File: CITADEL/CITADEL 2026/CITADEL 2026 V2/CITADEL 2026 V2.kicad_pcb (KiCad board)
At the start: 2 copper layers, 141.5 x 109.7 mm, 68 parts, among them J1 FAERIE CAN BUS, J10 ESC PWR, J13 SERVO DAUGHTER, J2 CITADEL CAN BUS, J3 FAERIE 12V, J4 CITADEL BATTERY, J5 FAERIE BATTERY, J6 LED STRIP, J7 CAMERA 1, J8 CAMERA 2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

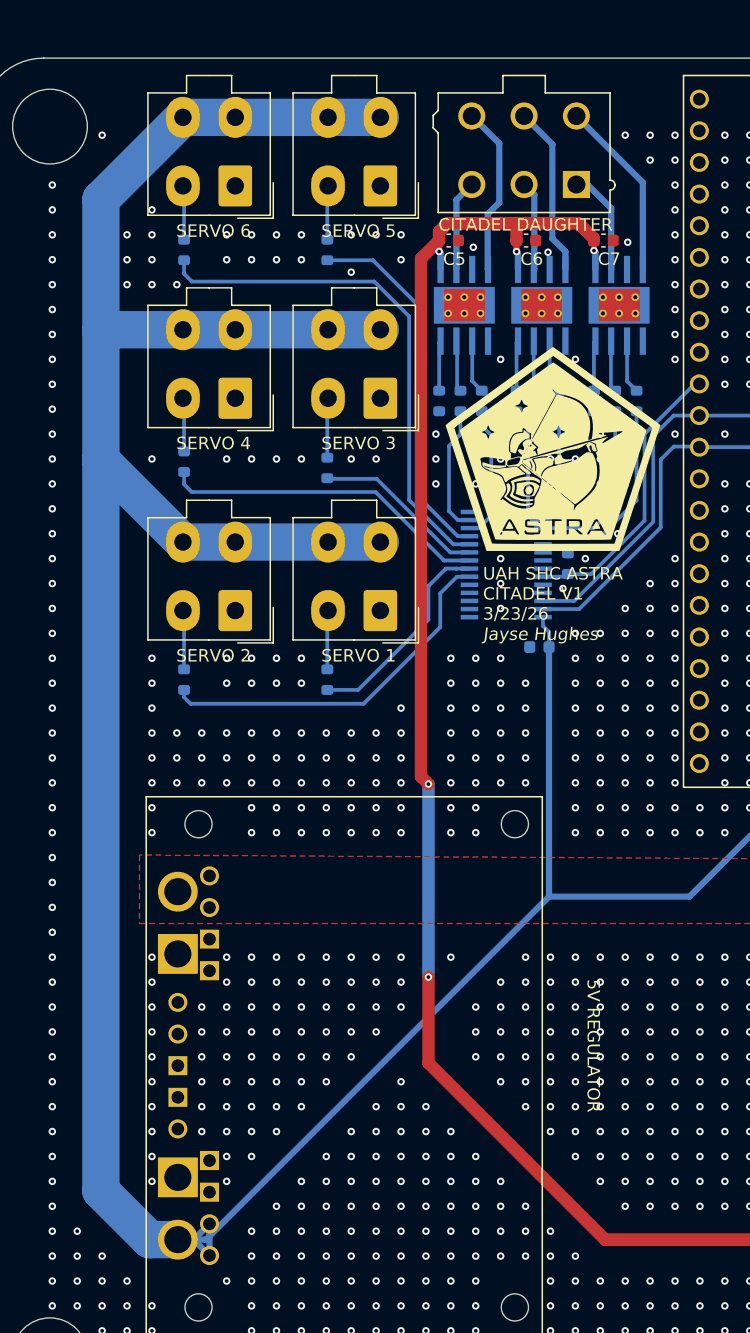
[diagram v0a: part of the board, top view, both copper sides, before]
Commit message: Changed linear actuator connectors
Removed the connector for the daughter board and moved the 1x2 molex connectors onto main board
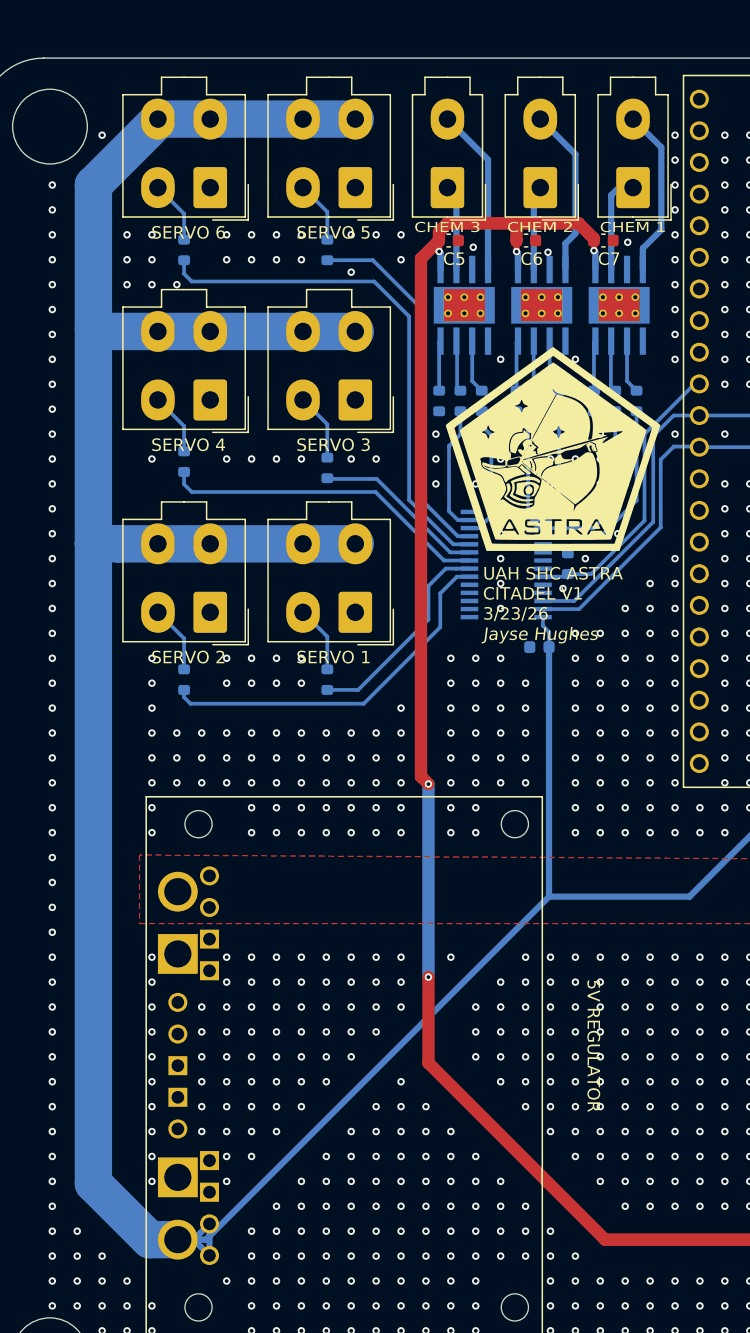
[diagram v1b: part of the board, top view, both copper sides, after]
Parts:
- added J11: CHEM 1, Connector_Molex:Molex_Mini-Fit_Jr_5566-02A_2x01_P4.20mm_Vertical, F.Cu at (73.6, 22.2)
- added J12: CHEM 2, Connector_Molex:Molex_Mini-Fit_Jr_5566-02A_2x01_P4.20mm_Vertical, F.Cu at (66.2, 22.2)
- J13: value SERVO DAUGHTER -> CHEM 3; footprint Jayse_Footprints:MOLEX_0039281063 -> Connector_Molex:Molex_Mini-Fit_Jr_5566-02A_2x01_P4.20mm_Vertical
- moved J13 6.76 mm to (58.7, 22.2)
- moved M1 2.01 mm to (51.3, 56.3)
- moved M3 2.01 mm to (51.3, 39.3)
- moved M5 2.01 mm to (51.3, 22.2)
- moved M2 2.01 mm to (39.7, 56.3)
- moved M4 2.01 mm to (39.7, 39.3)
- moved M6 2.01 mm to (39.7, 22.2)
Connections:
- J13 pad 1: /CHEM1_OUT1 -> /CHEM3_OUT1
- J13 pad 2: /CHEM2_OUT1 -> /CHEM3_OUT2
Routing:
- net +5V: track 397.6 -> 391.6 mm
- net /CHEM1_OUT2: track 14.5 -> 13.6 mm
- net /SERVO2: track 4.76 -> 5.45 mm
- net /SERVO6: track 4.36 -> 5.05 mm
- net /SERVO4: track 4.31 -> 5.00 mm
- net /SERVO5: track 4.35 -> 4.99 mm
- net /SERVO3: track 4.80 -> 5.44 mm
- net /SERVO1: track 4.75 -> 5.39 mm
- net /CHEM1_OUT1: track 8.50 -> 7.97 mm
- net GND: vias 1662 -> 1658
